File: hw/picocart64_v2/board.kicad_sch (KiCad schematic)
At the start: 79 parts, among them J1 USB_C_Receptacle_USB2.0, J2 USB_C_Receptacle_USB2.0, J3 Conn_02x06_Odd_Even, J4 Micro_SD_Card_Det, J5 Conn_01x02, J6 Conn_01x06, Q1 FDN340P, SW1 BootButton, SW2 ResetButton, U10 USBLC6-2SC6, U11 AZ1117-3.3, U12 N64-Cartridge, U14 RP2040, U15 RP2040, U16 ESP32-C3-WROOM-02, Y1 12MHz 10ppm, Y2 12MHz 10ppm

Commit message: New v2 board revision (v2.2) updated with help from Snipeye. Updated readme.
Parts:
- removed J2: USB_C_Receptacle_USB2.0, Connector_USB_Extra:USB_C_Receptacle_GT-USB-7010, symbol Connector:USB_C_Receptacle_USB2.0
- removed J5: Conn_01x02, project_area:PinHeader_1x08_P2.54mm_Vertical, symbol Connector_Generic:Conn_01x02
- removed J6: Conn_01x06, Connector_PinHeader_2.54mm:PinHeader_1x06_P2.54mm_Vertical, symbol Connector_Generic:Conn_01x06
- removed R10, R11: 22R, Resistor_SMD:R_0402_1005Metric, symbol Device:R_Small
- removed R3: 100k, Resistor_SMD:R_0402_1005Metric, symbol Device:R_Small
- removed RN1, RN2, RN3, RN4, RN5, RN6: 22R_x4, Resistor_SMD:R_Array_Convex_4x0603, symbol Device:R_Pack04
- added Q2: FDN340P, Package_TO_SOT_SMD:SOT-23, symbol Transistor_FET:FDN340P
- added R21, R22, R23, R24, R25, R26, R27, R28, R29, R30, R31, R32, R33, R34, R35, R36, R37, R38, R39, R40, R41, R42, R43, R44: 22R, Resistor_SMD:R_0402_1005Metric, symbol Device:R
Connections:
- net +3V3: now also U11.2 (VO)
- net AD0: now also R33.2
- net AD0': now also R33.1
- net AD1: now also R34.2
- net AD1': now also R34.1
- net AD10: now also R28.1
- net AD10': now also R28.2
- net AD11: now also R27.1
- net AD11': now also R27.2
- net AD12: now also R24.1
- net AD12': now also R24.2
- net AD13: now also R23.1
- net AD13': now also R23.2
- net AD14: now also R22.1
- net AD14': now also R22.2
- net AD15: now also R21.1
- net AD15': now also R21.2
- net AD2: now also R35.2
- net AD2': now also R35.1
- net AD3: now also R36.2
- net AD3': now also R36.1
- net AD4: now also R39.2
- net AD4': now also R39.1
- net AD5: now also R40.2
- net AD5': now also R40.1
- net AD6: now also R42.2
- net AD6': now also R42.1
- net AD7: now also R41.2
- net AD7': now also R41.1
- net AD8: now also R30.1
- net AD8': now also R30.2
- net AD9: now also R29.1
- net AD9': now also R29.2
- net ALEH: now also R38.2
- net ALEH': now also R38.1
- net ALEL: now also R37.2
- net ALEL': now also R37.1
- net CIC_DCLK: now also R43.2
- net CIC_DCLK': now also R43.1
- net CIC_DIO: now also R31.1
- net CIC_DIO': now also R31.2
- net N64_VCC: now also Q2.2 (S); no longer Q1.3 (D)
- net VBUS: now also Q1.1 (G), R20.2, Q2.1 (G)
- net ~{COLD_RESET'}: now also R32.2
- net ~{COLD_RESET}: now also R32.1
- net ~{INT1'}: now also R44.1
- net ~{INT1}: now also R44.2
- net ~{READ'}: now also R26.2
- net ~{READ}: now also R26.1
- net ~{WRITE'}: now also R25.2
- net ~{WRITE}: now also R25.1
- removed net 3V3_USB: Q1.1 (G), R20.2, U11.2 (VO)
- new net: Q1.3 (D), Q2.3 (D)
- no-connect marks 25 -> 21
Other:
- note removed: "DNP - For extra debug/evaluation only CC resistors omitted for simplicity"
- note removed: "Project Area"
- moved on the sheet: C11, C12, C13, C14, C15, C16, C17, C18, C19, C20, C21, C22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

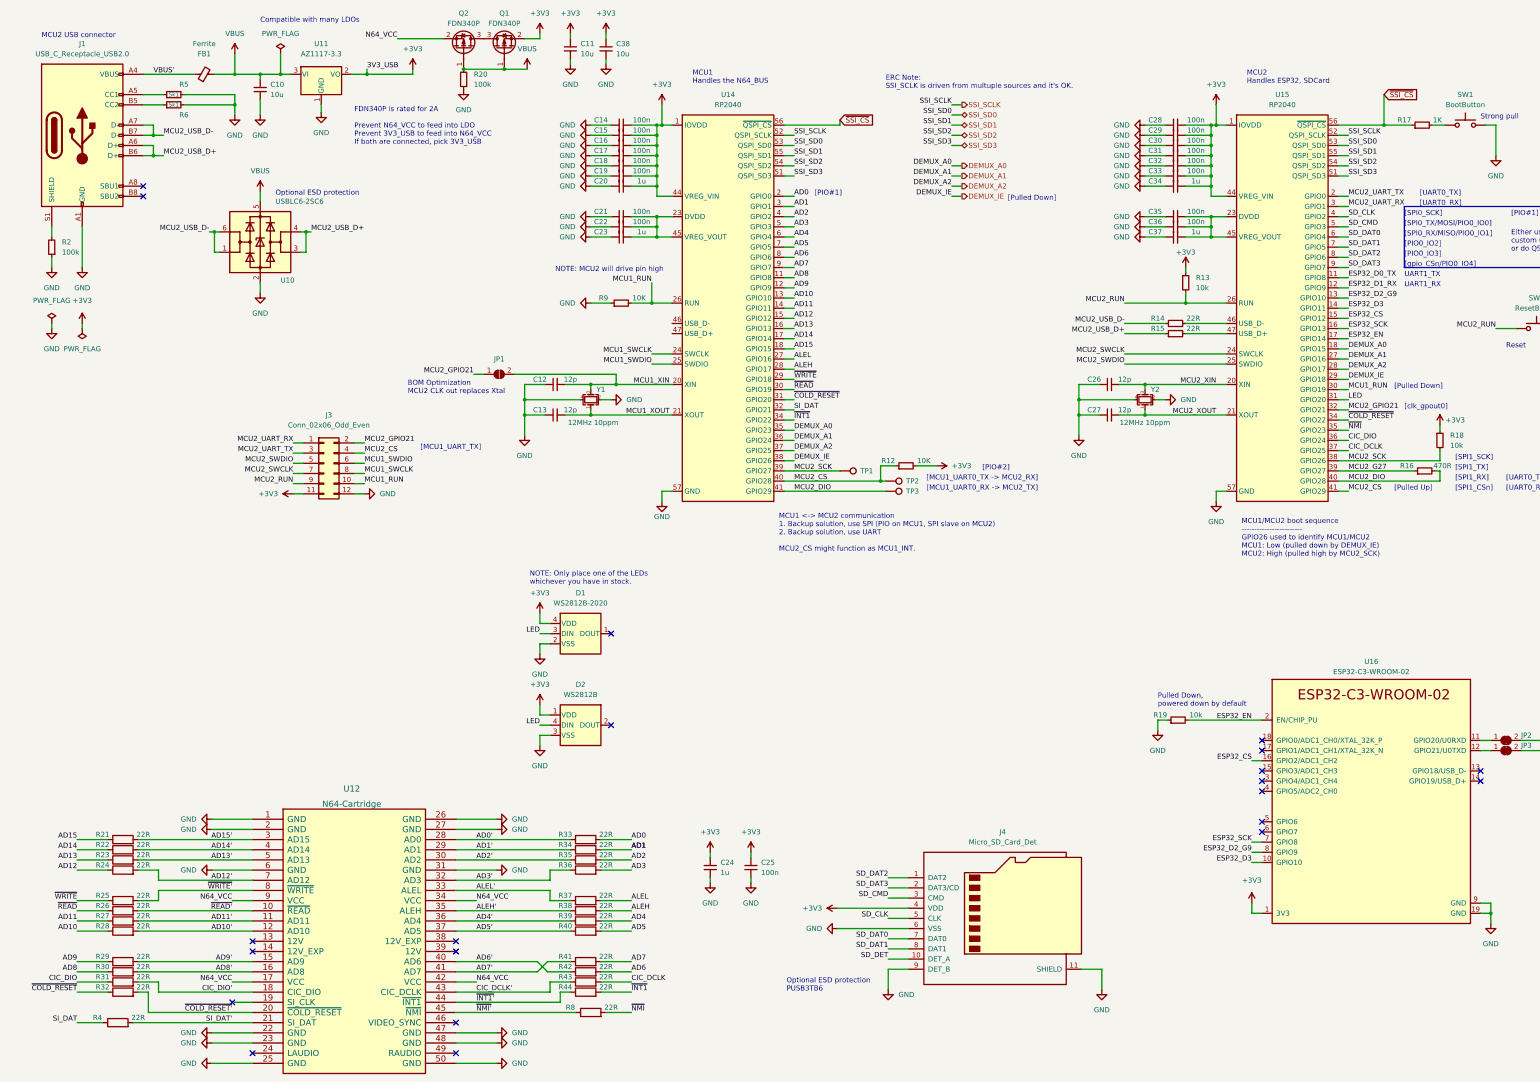
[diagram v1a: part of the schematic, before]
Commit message: Updated v2 pcb to use a tristate buffer to toggle between boot flash and psram array.
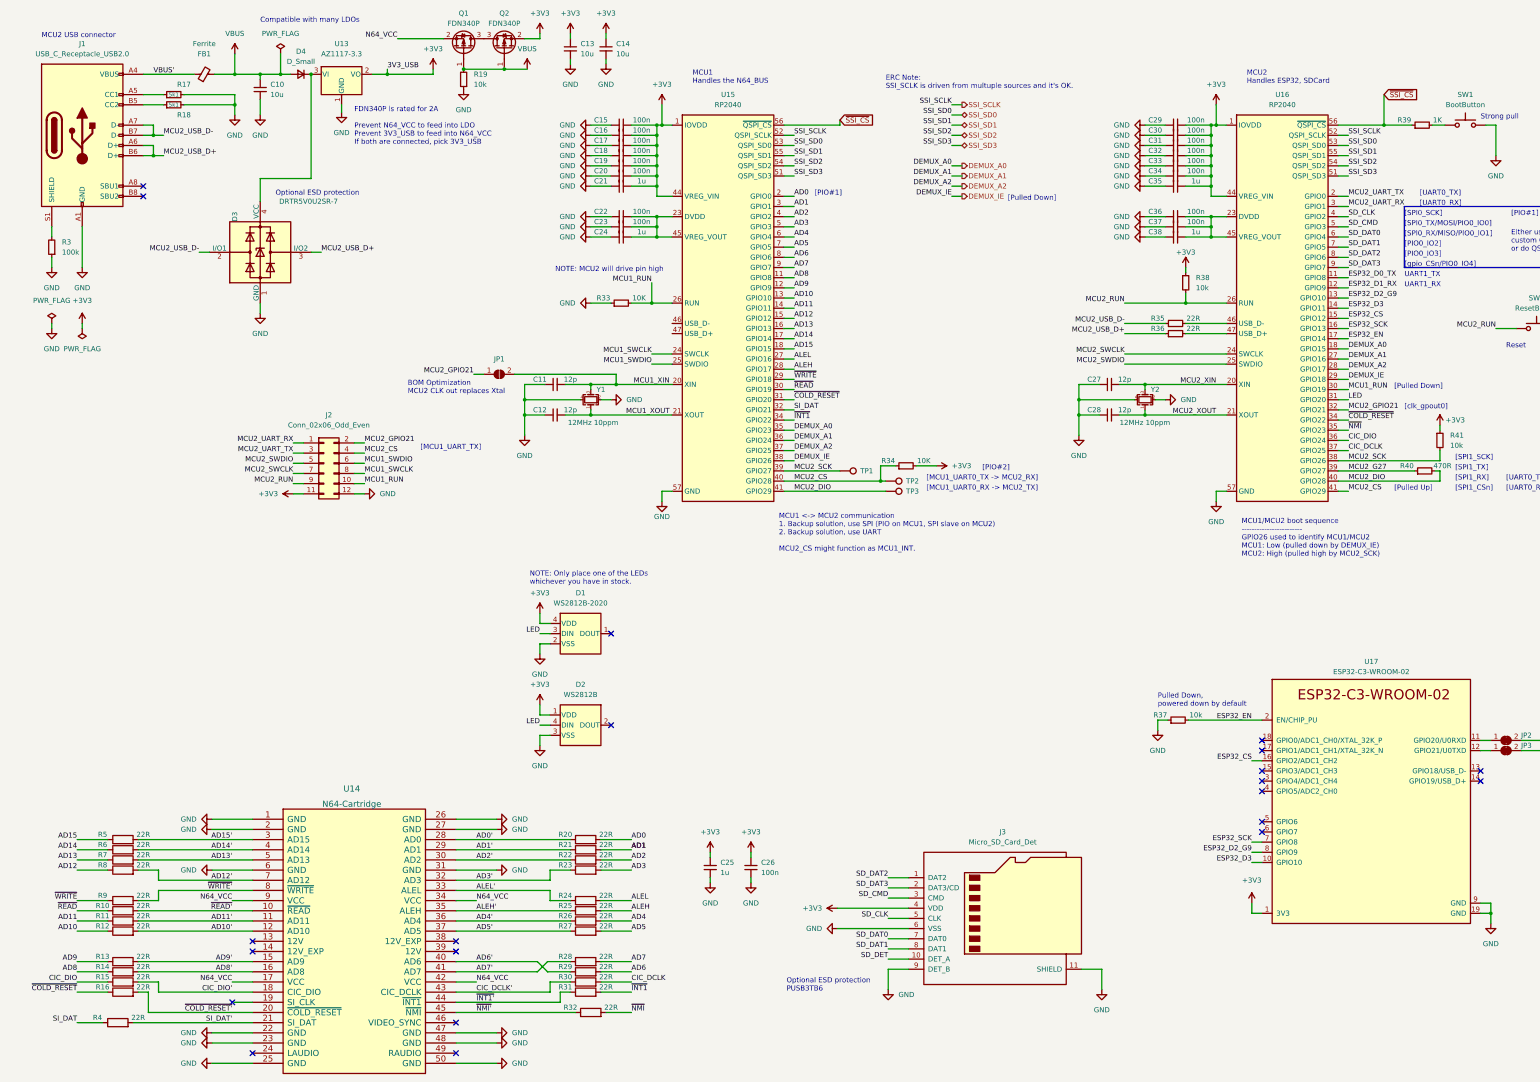
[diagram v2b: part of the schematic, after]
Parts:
- removed U10: USBLC6-2SC6, Package_TO_SOT_SMD:SOT-666, symbol Power_Protection:USBLC6-2SC6
- added D3: DRTR5V0U2SR-7, Package_TO_SOT_SMD:SOT-143, symbol Power_Protection:PRTR5V0U2X
- added D4: D_Small, Diode_SMD:D_SMA, symbol Device:D_Small
- R19: renamed from R20; value 100k -> 10k
- renumbered C12 to C11, C13 to C12, C11 to C13, C38 to C14, C14 to C15, C15 to C16, C16 to C17, C17 to C18, C18 to C19, C19 to C20, C20 to C21, C21 to C22, C22 to C23, C23 to C24, C24 to C25, C25 to C26, C26 to C27, C27 to C28, C28 to C29, C29 to C30, C30 to C31, C31 to C32, C32 to C33, C33 to C34, C34 to C35, C35 to C36, C36 to C37, C37 to C38, J3 to J2, J4 to J3, Q2 to Q1, Q1 to Q2, R26 to R10, R27 to R11, R28 to R12, R29 to R13, R30 to R14, R31 to R15, R32 to R16, R5 to R17, R6 to R18, R33 to R20, R34 to R21, R35 to R22, R36 to R23, R37 to R24, R38 to R25, R39 to R26, R40 to R27, R41 to R28, R42 to R29, R2 to R3, R43 to R30, R44 to R31, R8 to R32, R9 to R33, R12 to R34, R14 to R35, R15 to R36, R19 to R37, R13 to R38, R17 to R39, R16 to R40, R18 to R41, R21 to R5, R22 to R6, R23 to R7, R24 to R8, R25 to R9, U11 to U13, U12 to U14, U14 to U15, U15 to U16, U16 to U17
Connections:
- net GND: now also D3.1 (GND)
- net MCU2_USB_D+: now also D3.3 (I/O2)
- net MCU2_USB_D-: now also D3.2 (I/O1)
- net VBUS: now also D4.2 (A); no longer U13.3 (VI)
- new net: D3.4 (VCC), D4.1 (K), U13.3 (VI)
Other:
- moved on the sheet: U13

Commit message: Updated hardware files
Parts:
- added C48, C49, C50, C51, C52, C53, C54, C55, C56, C57: 100n, Capacitor_SMD:C_0402_1005Metric, symbol Device:C_Small
- added R42, R43, R44, R45, R46, R47, R48, R49, R50, R51, R52, R53, R54, R55, R56, R57, R58, R59, R60, R61: R, Resistor_SMD:R_0402_1005Metric, symbol Device:R_Small
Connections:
- net +3V3: now also C48.1, C49.1, C50.1, C51.1, C52.1, C53.1, C54.1, C55.1, C56.1, C57.1, R42.2, R43.2, R46.2, R47.2, R50.2, R51.2, R54.2, R55.2, R58.2, R59.2
- net GND: now also C48.2, C49.2, C50.2, C51.2, C52.2, C53.2, C54.2, C55.2, C56.2, C57.2, R44.1, R45.1, R48.1, R49.1, R52.1, R53.1, R56.1, R57.1, R60.1, R61.1
- net SSI_SCLK: now also R42.1, R43.1, R44.2, R45.2
- net SSI_SD0: now also R46.1, R47.1, R48.2, R49.2
- net SSI_SD1: now also R50.1, R51.1, R52.2, R53.2
- net SSI_SD2: now also R54.1, R55.1, R56.2, R57.2
- net SSI_SD3: now also R58.1, R59.1, R60.2, R61.2
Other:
- note added: "Some Thevenin terminating resistor pads near each MCU are useful if we need to improve signal integrity at high QSPI clocks"

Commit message: Updated schematic to include a chin for the USB port and slightly increased the length of the SD Card chin. This should help it be more accessible once inside a shell. Updated schematic to include part numbers for all the components.
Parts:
- C10, C13, C14: LCSC (none) -> C15525
- C11, C12, C27, C28: LCSC (none) -> C106201
- C15, C16, C17, C18, C19, C20, C22, C23, C26, C29, C30, C31, C32, C33, C34, C36, C37, C48, C49, C50, C51, C52, C53, C54, C55, C56, C57: LCSC (none) -> C1525
- C21, C24, C25, C35, C38: LCSC (none) -> C14445
- D1: LCSC (none) -> C965555
- D2: LCSC (none) -> C114586
- FB1: LCSC (none) -> C76892
- J1: LCSC (none) -> C136423
- J3: LCSC (none) -> C585350
- R10, R11, R12, R13, R14, R15, R16, R20, R21, R22, R23, R24, R25, R26, R27, R28, R29, R30, R31, R32, R35, R36, R4, R5, R6, R7, R8, R9: LCSC (none) -> C409710
- R17, R18: LCSC (none) -> C105873
- R19, R33, R34, R37, R38, R41: LCSC (none) -> C406733
- R3: LCSC (none) -> C25741
- R39: LCSC (none) -> C105637
- R40: LCSC (none) -> C25117
- R42, R43, R44, R45, R46, R47, R48, R49, R50, R51, R52, R53, R54, R55, R56, R57, R58, R59, R60, R61: value R -> 1K; LCSC (none) -> C105637
- SW1, SW2: LCSC (none) -> C318938
- U13: LCSC (none) -> C108495
- U15, U16: LCSC (none) -> C2040
- U17: LCSC (none) -> C2934560
